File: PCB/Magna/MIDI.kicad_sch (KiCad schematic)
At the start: 14 parts, among them J1001 DIN-5_180degree, J1002 DIN-5_180degree, J1003 DIN-5_180degree, U1001 74HC08D, U1002 6N137

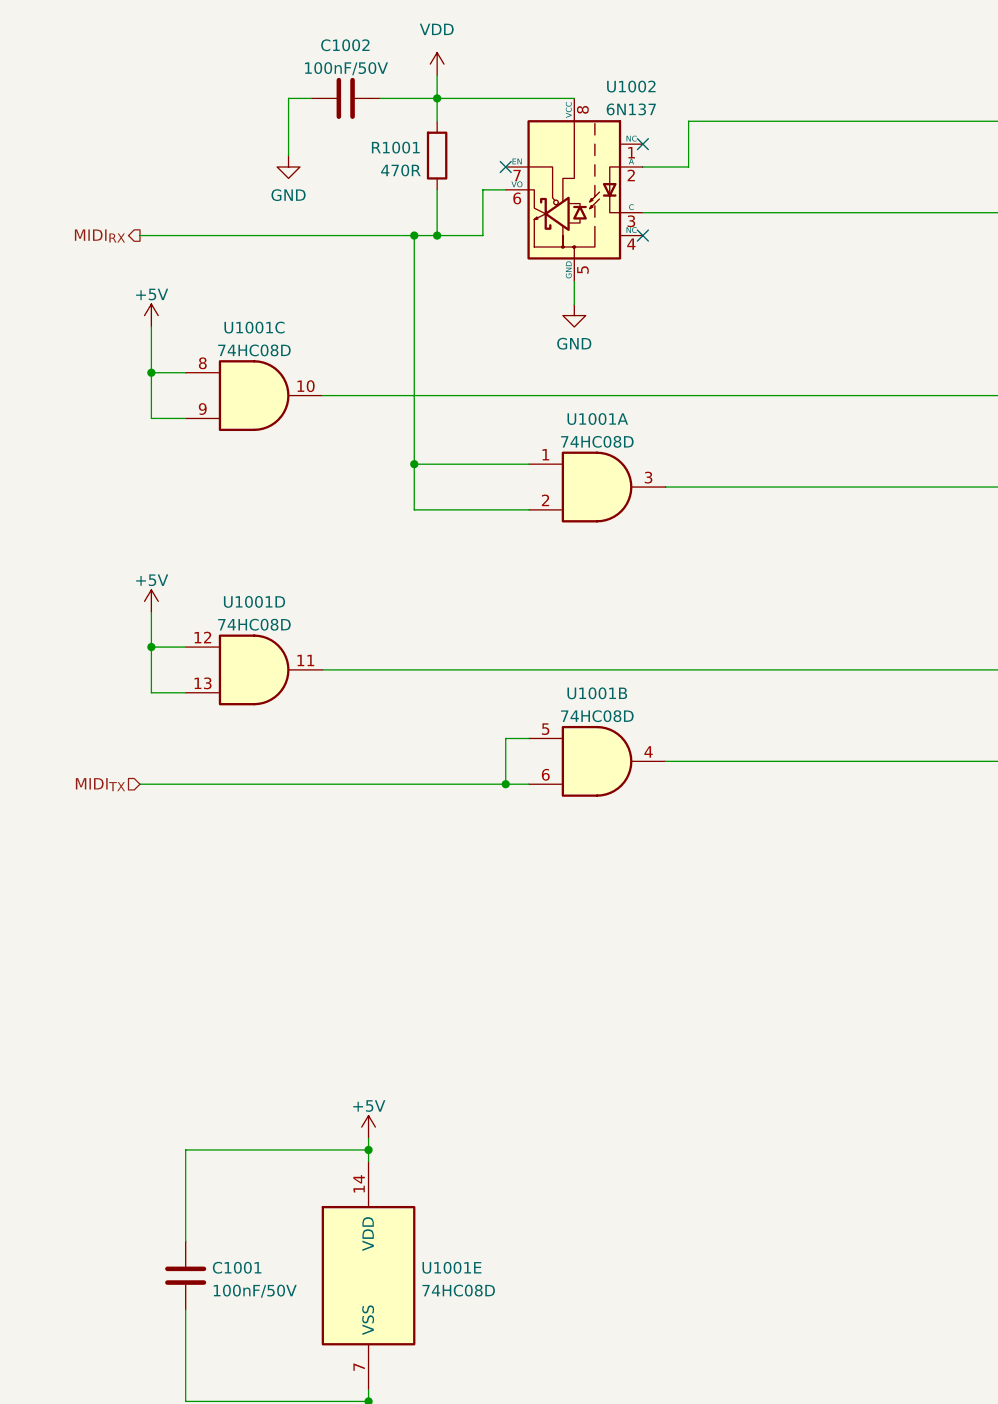
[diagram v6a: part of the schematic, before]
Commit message: Split schematic to several projects
To allow for several boards to be done a kicad project
is needed for each
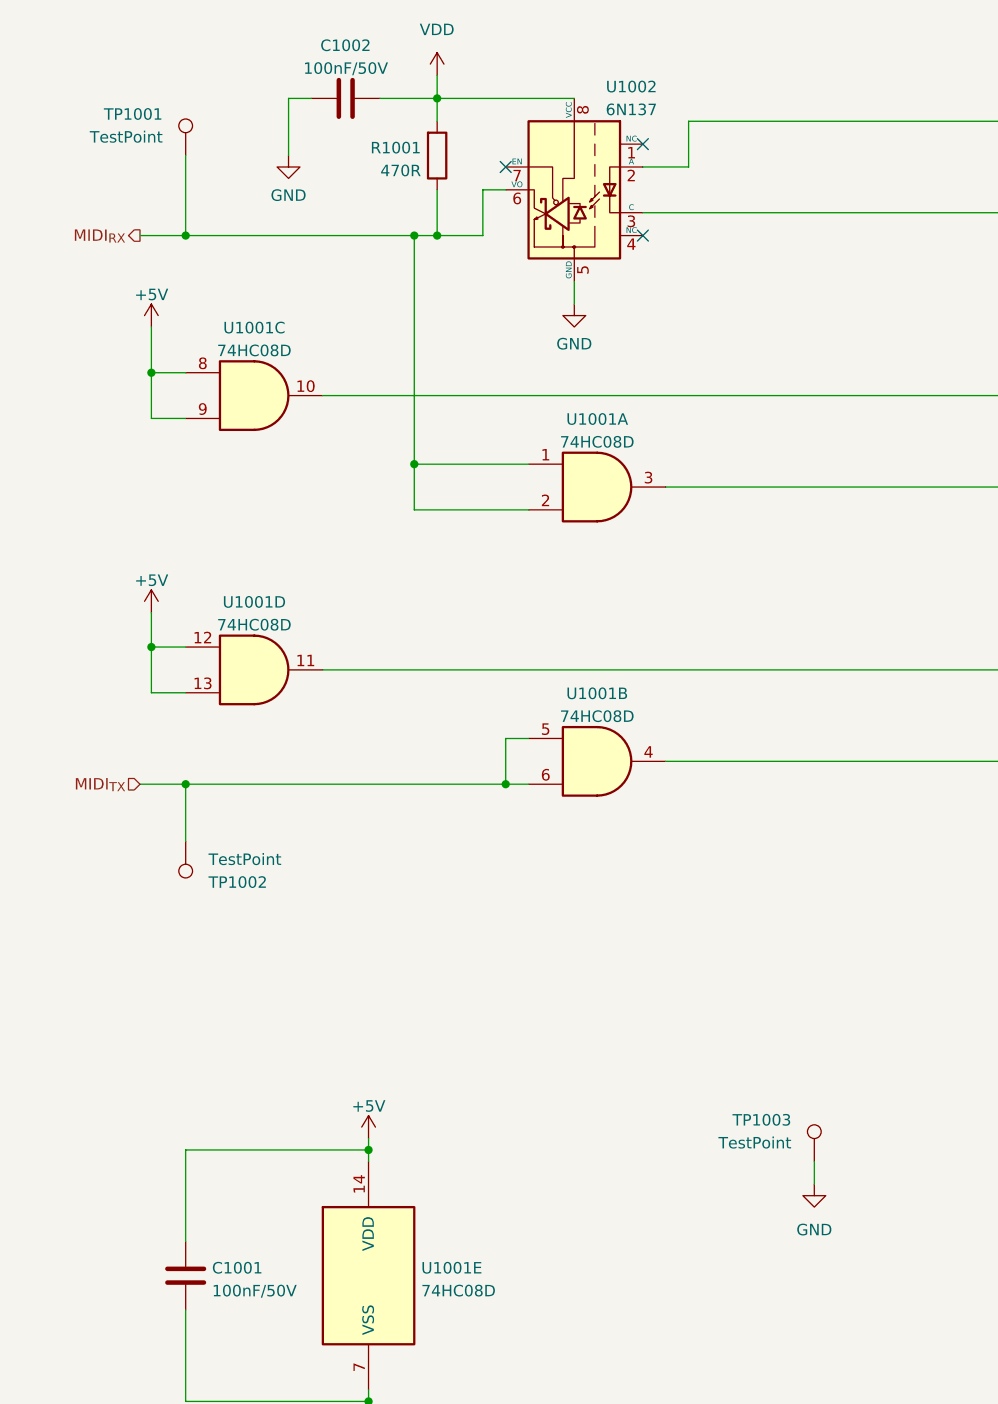
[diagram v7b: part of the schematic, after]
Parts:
- added TP1001, TP1002, TP1003: TestPoint, TestPoint:TestPoint_Keystone_5005-5009_Compact, symbol Connector:TestPoint
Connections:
- net GND: now also TP1003.1
- net MIDI_{RX}: now also TP1001.1
- net MIDI_{TX}: now also TP1002.1
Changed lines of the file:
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@@
 (kicad_sch (version 20230121) (generator eeschema)
   (paper "A4")
+  (junction (at 43.18 43.18) (diameter 0) (color 0 0 0 0)
+  )
   (junction (at 63.5 172.72) (diameter 0) (color 0 0 0 0)
   )
@@
   )
   (junction (at 71.12 43.18) (diameter 0) (color 0 0 0 0)
+  )
+  (junction (at 43.18 104.14) (diameter 0) (color 0 0 0 0)
   )
   (junction (at 63.5 144.78) (diameter 0) (color 0 0 0 0)
@@
     (stroke (width 0) (type default))
   )
+  (wire (pts (xy 43.18 104.14) (xy 43.18 110.49))
+    (stroke (width 0) (type default))
+  )
   (wire (pts (xy 76.2 38.1) (xy 78.74 38.1))
     (stroke (width 0) (type default))
@@
     (stroke (width 0) (type default))
   )
-  (wire (pts (xy 38.1 104.14) (xy 78.74 104.14))
+  (wire (pts (xy 38.1 104.14) (xy 43.18 104.14))
     (stroke (width 0) (type default))
   )
@@
     (stroke (width 0) (type default))
   )
+  (wire (pts (xy 113.03 148.59) (xy 113.03 146.05))
+    (stroke (width 0) (type default))
+  )
   (wire (pts (xy 96.52 101.6) (xy 193.04 101.6))
     (stroke (width 0) (type default))
@@
     (stroke (width 0) (type default))
   )
-  (wire (pts (xy 38.1 43.18) (xy 68.58 43.18))
+  (wire (pts (xy 43.18 43.18) (xy 68.58 43.18))
+    (stroke (width 0) (type default))
+  )
+  (wire (pts (xy 38.1 43.18) (xy 43.18 43.18))
     (stroke (width 0) (type default))
   )
@@
     (stroke (width 0) (type default))
   )
+  (wire (pts (xy 43.18 34.29) (xy 43.18 43.18))
+    (stroke (width 0) (type default))
+  )
   (wire (pts (xy 43.18 88.9) (xy 39.37 88.9))
+    (stroke (width 0) (type default))
+  )
+  (wire (pts (xy 43.18 104.14) (xy 78.74 104.14))
     (stroke (width 0) (type default))
   )
@@
         (path "/f86ff50f-706c-4b52-a083-2f7e8e3afb1c/6a61af6a-88ef-4b64-8aa8-4a34e80ee921"
           (reference "#R?") (unit 1)
+        )
+      )
+    )
+  )
+  (symbol (lib_id "power:GND") (at 113.03 148.59 0) (unit 1)
+    (in_bom yes) (on_board yes) (dnp no)
+    (property "Reference" "#PWR01008" (at 113.03 154.94 0)
+      (effects (font (size 1.27 1.27)) hide)
+    )
+    (property "Value" "GND" (at 113.03 153.67 0)
+      (effects (font (size 1.27 1.27)))
+    )
+    (property "Footprint" "" (at 113.03 148.59 0)
+      (effects (font (size 1.27 1.27)) hide)
+    )
+    (property "Datasheet" "" (at 113.03 148.59 0)
+      (effects (font (size 1.27 1.27)) hide)
+    )
+    (pin "1")
+    (instances
+      (project "Magna"
+        (path "/1469ea1f-a157-49dc-a369-2d42fa17695d/93ffa52a-dd6e-48b1-81f9-f219879f28f9"
+          (reference "#PWR01008") (unit 1)
         )
       )
@@
     )
   )
+  (symbol (lib_id "Connector:TestPoint") (at 43.18 34.29 0) (mirror y) (unit 1)
+    (in_bom yes) (on_board yes) (dnp no)
+    (property "Reference" "TP1001" (at 40.64 29.718 0)
+      (effects (font (size 1.27 1.27)) (justify left))
+    )
+    (property "Value" "TestPoint" (at 40.64 32.258 0)
+      (effects (font (size 1.27 1.27)) (justify left))
+    )
+    (property "Footprint" "TestPoint:TestPoint_Keystone_5005-5009_Compact" (at 38.1 34.29 0)
+      (effects (font (size 1.27 1.27)) hide)
+    )
+    (property "Datasheet" "~" (at 38.1 34.29 0)
+      (effects (font (size 1.27 1.27)) hide)
+    )
+    (pin "1")
+    (instances
+      (project "Magna"
+        (path "/1469ea1f-a157-49dc-a369-2d42fa17695d/93ffa52a-dd6e-48b1-81f9-f219879f28f9"
+          (reference "TP1001") (unit 1)
+        )
+      )
+    )
+  )
   (symbol (lib_id "Device:R") (at 196.85 101.6 90) (unit 1)
     (in_bom yes) (on_board yes) (dnp no) (fields_autoplaced)
@@
   (symbol (lib_id "Skrooter_symbols:SHIELD") (at 269.24 99.06 0) (unit 1)
     (in_bom yes) (on_board yes) (dnp no) (fields_autoplaced)
-    (property "Reference" "#PWR01009" (at 269.24 104.14 0)
+    (property "Reference" "#PWR01010" (at 269.24 104.14 0)
       (effects (font (size 1.27 1.27)) hide)
     )
@@
       (project "Magna"
         (path "/1469ea1f-a157-49dc-a369-2d42fa17695d/93ffa52a-dd6e-48b1-81f9-f219879f28f9"
-          (reference "#PWR01009") (unit 1)
+          (reference "#PWR01010") (unit 1)
         )
       )
@@
     )
   )
+  (symbol (lib_id "Connector:TestPoint") (at 43.18 110.49 0) (mirror x) (unit 1)
+    (in_bom yes) (on_board yes) (dnp no)
+    (property "Reference" "TP1002" (at 45.72 115.062 0)
+      (effects (font (size 1.27 1.27)) (justify left))
+    )
+    (property "Value" "TestPoint" (at 45.72 112.522 0)
+      (effects (font (size 1.27 1.27)) (justify left))
+    )
+    (property "Footprint" "TestPoint:TestPoint_Keystone_5005-5009_Compact" (at 48.26 110.49 0)
+      (effects (font (size 1.27 1.27)) hide)
+    )
+    (property "Datasheet" "~" (at 48.26 110.49 0)
+      (effects (font (size 1.27 1.27)) hide)
+    )
+    (pin "1")
+    (instances
+      (project "Magna"
+        (path "/1469ea1f-a157-49dc-a369-2d42fa17695d/93ffa52a-dd6e-48b1-81f9-f219879f28f9"
+          (reference "TP1002") (unit 1)
+        )
+      )
+    )
+  )
   (symbol (lib_id "power:+5V") (at 63.5 143.51 0) (unit 1)
     (in_bom yes) (on_board yes) (dnp no) (fields_autoplaced)
@@
   (symbol (lib_id "Skrooter_symbols:SHIELD") (at 269.24 68.58 0) (unit 1)
     (in_bom yes) (on_board yes) (dnp no) (fields_autoplaced)
-    (property "Reference" "#PWR01008" (at 269.24 73.66 0)
+    (property "Reference" "#PWR01009" (at 269.24 73.66 0)
       (effects (font (size 1.27 1.27)) hide)
     )
@@
       (project "Magna"
         (path "/1469ea1f-a157-49dc-a369-2d42fa17695d/93ffa52a-dd6e-48b1-81f9-f219879f28f9"
-          (reference "#PWR01008") (unit 1)
+          (reference "#PWR01009") (unit 1)
         )
       )
@@
         )
       )
+    )
+  )
+  (symbol (lib_id "Connector:TestPoint") (at 113.03 146.05 0) (unit 1)
+    (in_bom yes) (on_board yes) (dnp no)
+    (property "Reference" "TP1003" (at 110.49 141.478 0)
+      (effects (font (size 1.27 1.27)) (justify right))
+    )
+    (property "Value" "TestPoint" (at 110.49 144.018 0)
+      (effects (font (size 1.27 1.27)) (justify right))
+    )
+    (property "Footprint" "TestPoint:TestPoint_Keystone_5005-5009_Compact" (at 118.11 146.05 0)
+      (effects (font (size 1.27 1.27)) hide)
+    )
+    (property "Datasheet" "~" (at 118.11 146.05 0)
+      (effects (font (size 1.27 1.27)) hide)
+    )
+    (pin "1")
+    (instances
+      (project "Magna"
+        (path "/1469ea1f-a157-49dc-a369-2d42fa17695d/93ffa52a-dd6e-48b1-81f9-f219879f28f9"
+          (reference "TP1003") (unit 1)
+        )
+      )
